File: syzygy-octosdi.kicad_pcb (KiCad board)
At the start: 4 copper layers, 100 x 50 mm, 211 parts, among them CN1 QTH-020-01-F-D-DP-A, J1 Conn_Coaxial, J2 Conn_Coaxial, J3 Conn_Coaxial, J4 Conn_Coaxial, J5 Conn_Coaxial, J6 Conn_Coaxial, J7 Conn_Coaxial, J8 Conn_Coaxial, J9 Conn_02x03_Odd_Even, U1 LMH0344SQE_NOPB, U10 GS2988-INE3, U11 STM32G031G8Ux, U2 LMH0344SQE_NOPB, U3 LMH0344SQE_NOPB, U4 LMH0344SQE_NOPB, U5 PCAL6416AHF, U6 PCAL6416AHF, U7 GS2988-INE3, U8 GS2988-INE3, U9 GS2988-INE3, X1 SX7DF148_500B20F30DNN

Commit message: finish routing
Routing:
- net +3V3: track 577.3 -> 703.0 mm, vias 48 -> 46
- net GND: track 137.2 -> 142.4 mm
- net /Outputs/SDI Out 3/SD/~{HD}: track 13.0 -> 14.6 mm

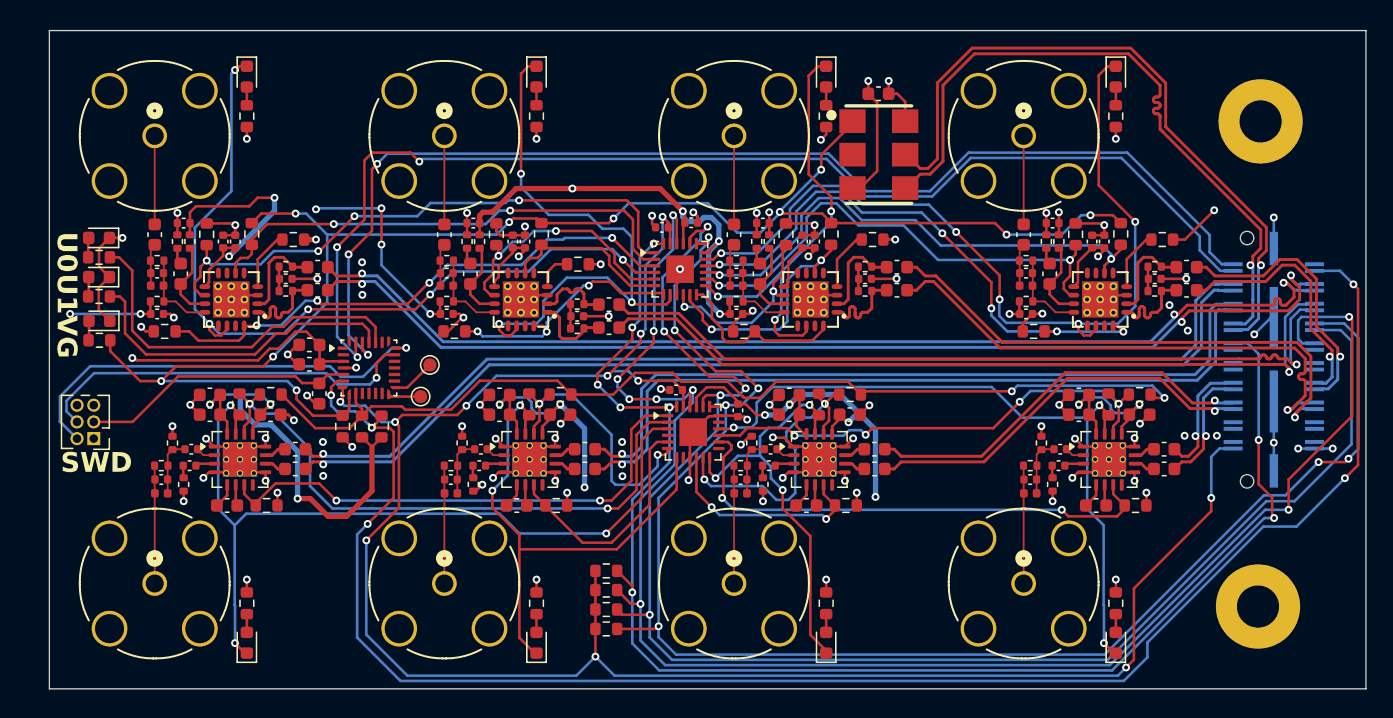
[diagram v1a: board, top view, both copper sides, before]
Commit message: fixes following review and more mounting holes
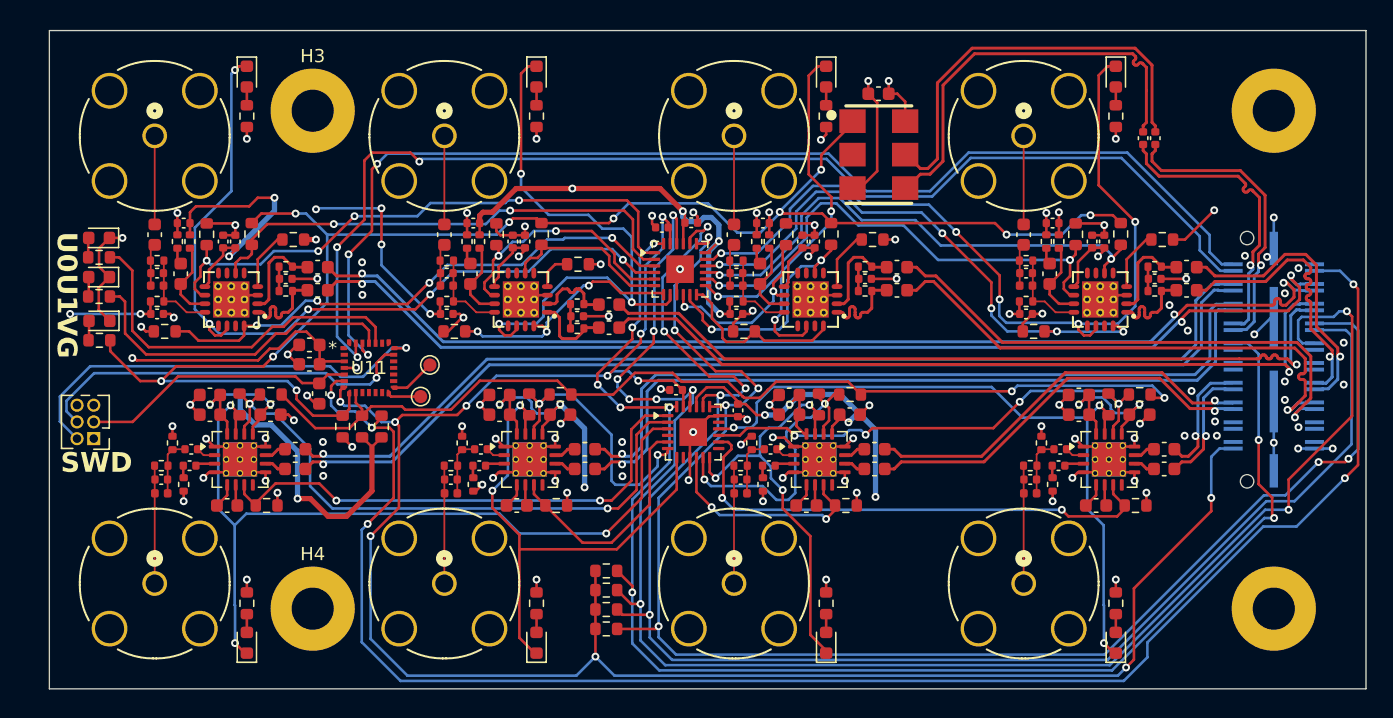
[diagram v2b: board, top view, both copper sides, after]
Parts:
- added C85: 10n, Capacitor_SMD:C_0402_1005Metric, F.Cu at (134.0, 58.2)
- added C86: 10n, Capacitor_SMD:C_0402_1005Metric, F.Cu at (133.1, 58.2)
- added H3: MountingHole_Pad, MountingHole:MountingHole_3.2mm_M3_Pad, F.Cu at (70.0, 56.1)
- added H4: MountingHole_Pad, MountingHole:MountingHole_3.2mm_M3_Pad, F.Cu at (70.0, 93.9)
- R36, R47, R58, R69: value 750 -> 750 1%
- U11: footprint Package_DFN_QFN:QFN-28_4x4mm_P0.5mm -> JLCImport:UFQFPN-28_STM
- moved H2 1.29 mm to (143.0, 56.1)
- moved H1 1.21 mm to (143.0, 93.9)
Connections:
- X1 pad 4: /REFCLK.P -> /REF+
- X1 pad 5: /REFCLK.N -> /REF-
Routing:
- net /REF-: track 0.00 -> 32.1 mm
- net /REF+: track 0.00 -> 32.0 mm
- net /REFCLK.N: track 52.3 -> 22.7 mm
- net /REFCLK.P: track 52.2 -> 22.7 mm
- net +3V3: track 703.0 -> 698.9 mm
- net /TX3.P: track 19.6 -> 21.9 mm
- net /TX3.N: track 21.0 -> 22.0 mm
- net GND: vias 78 -> 90

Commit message: add power led and test points
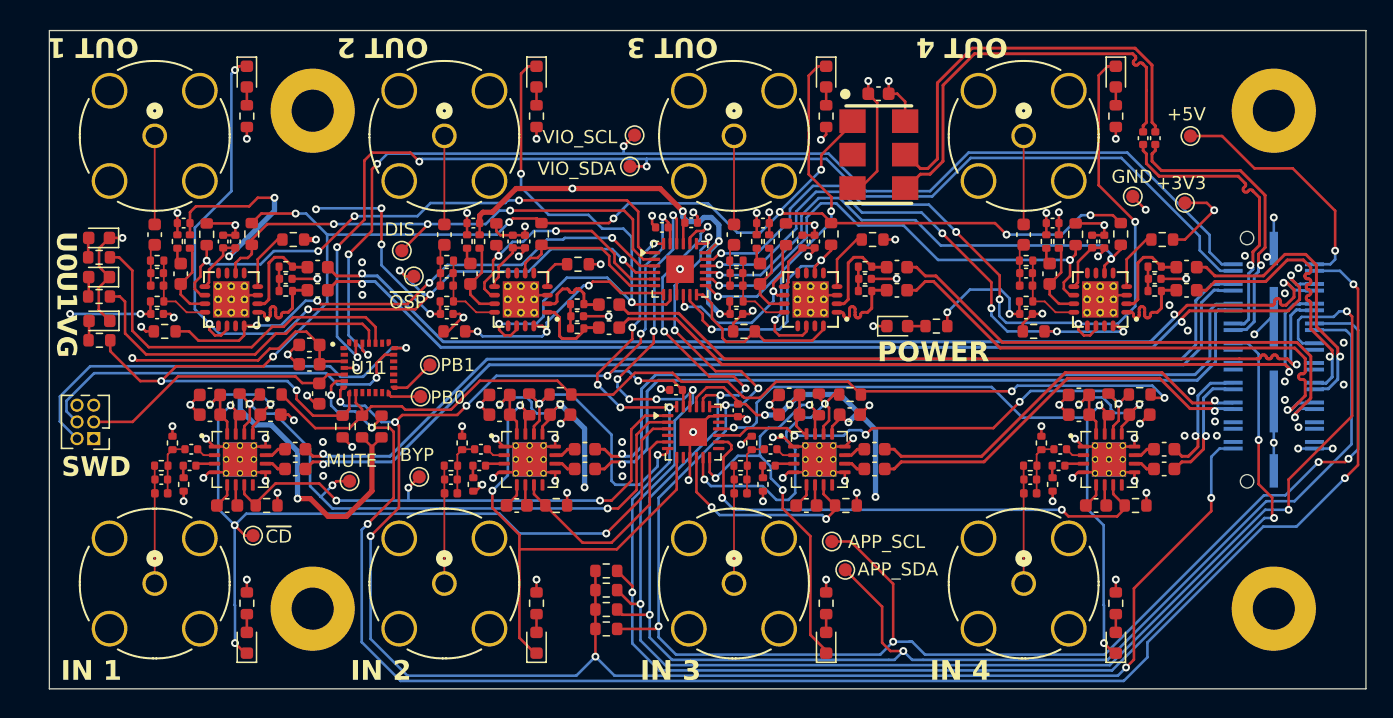
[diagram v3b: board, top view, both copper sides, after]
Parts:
- added D1: LED, LED_SMD:LED_0603_1608Metric, F.Cu at (114.4, 72.5)
- added R1: 1k, Resistor_SMD:R_0603_1608Metric, F.Cu at (117.4, 72.5)
- added TP1: TestPoint, TestPoint:TestPoint_Pad_D1.0mm, F.Cu at (109.4, 88.8)
- added TP10: TestPoint, TestPoint:TestPoint_Pad_D1.0mm, F.Cu at (65.5, 88.4)
- added TP11: TestPoint, TestPoint:TestPoint_Pad_D1.0mm, F.Cu at (76.8, 66.7)
- added TP12: TestPoint, TestPoint:TestPoint_Pad_D1.0mm, F.Cu at (77.7, 68.7)
- added TP2: TestPoint, TestPoint:TestPoint_Pad_D1.0mm, F.Cu at (94.5, 58.0)
- added TP3: TestPoint, TestPoint:TestPoint_Pad_D1.0mm, F.Cu at (94.1, 60.3)
- added TP4: TestPoint, TestPoint:TestPoint_Pad_D1.0mm, F.Cu at (136.7, 58.0)
- added TP5: TestPoint, TestPoint:TestPoint_Pad_D1.0mm, F.Cu at (136.2, 63.1)
- added TP6: TestPoint, TestPoint:TestPoint_Pad_D1.0mm, F.Cu at (132.3, 62.6)
- added TP7: TestPoint, TestPoint:TestPoint_Pad_D1.0mm, F.Cu at (110.5, 91.0)
- added TP8: TestPoint, TestPoint:TestPoint_Pad_D1.0mm, F.Cu at (78.1, 83.9)
- added TP9: TestPoint, TestPoint:TestPoint_Pad_D1.0mm, F.Cu at (72.8, 84.2)
- renumbered C85 to C1, C8 to C10, C9 to C11, C10 to C12, C11 to C13, C12 to C14, C13 to C15, C14 to C16, C15 to C17, C16 to C18, C17 to C19, C86 to C2, C18 to C20, C19 to C21, C20 to C22, C21 to C23, C22 to C24, C23 to C25, C24 to C26, C25 to C27, C26 to C28, C27 to C29, C1 to C3, C28 to C30, C29 to C31, C30 to C32, C31 to C33, C32 to C34, C33 to C35, C34 to C36, C35 to C37, C36 to C38, C37 to C39, C2 to C4, C38 to C40, C39 to C41, C40 to C42, C41 to C43, C42 to C44, C43 to C45, C44 to C46, C45 to C47, C46 to C48, C47 to C49, C3 to C5, C48 to C50, C49 to C51, C50 to C52, C51 to C53, C52 to C54, C53 to C55, C54 to C56, C55 to C57, C56 to C58, C57 to C59, C4 to C6, C58 to C60, C59 to C61, C60 to C62, C61 to C63, C62 to C64, C63 to C65, C64 to C66, C65 to C67, C66 to C68, C67 to C69, C5 to C7, C68 to C70, C69 to C71, C70 to C72, C71 to C73, C72 to C74, C73 to C75, C74 to C76, C75 to C77, C76 to C78, C77 to C79, C6 to C8, C78 to C80, C79 to C81, C80 to C82, C81 to C83, C82 to C84, C83 to C85, C84 to C86, C7 to C9, D9 to D10, D10 to D11, D11 to D12, D1 to D2, D2 to D3, D3 to D4, D4 to D5, D5 to D6, D6 to D7, D7 to D8, D8 to D9, H3 to H2, H2 to H3, R9 to R10, R10 to R11, R11 to R12, R12 to R13, R13 to R14, R14 to R15, R15 to R16, R16 to R17, R17 to R18, R18 to R19, R1 to R2, R19 to R20, R20 to R21, R21 to R22, R22 to R23, R23 to R24, R24 to R25, R25 to R26, R26 to R27, R27 to R28, R28 to R29, R2 to R3, R29 to R30, R30 to R31, R31 to R32, R32 to R33, R33 to R34, R34 to R35, R35 to R36, R36 to R37, R37 to R38, R38 to R39, R3 to R4, R39 to R40, R40 to R41, R41 to R42, R42 to R43, R43 to R44, R44 to R45, R45 to R46, R46 to R47, R47 to R48, R48 to R49, R4 to R5, R49 to R50, R50 to R51, R51 to R52, R52 to R53, R53 to R54, R54 to R55, R55 to R56, R56 to R57, R57 to R58, R58 to R59, R5 to R6, R59 to R60, R60 to R61, R61 to R62, R62 to R63, R63 to R64, R64 to R65, R65 to R66, R66 to R67, R67 to R68, R68 to R69, R6 to R7, R69 to R70, R70 to R71, R71 to R72, R72 to R73, R73 to R74, R74 to R75, R75 to R76, R76 to R77, R77 to R78, R78 to R79, R7 to R8, R79 to R80, R80 to R81, R81 to R82, R82 to R83, R8 to R9, TP1 to TP13, TP2 to TP14
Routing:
- net +5V: track 0.00 -> 18.8 mm, vias 0 -> 1
- net /I2C.SCL: track 117.6 -> 128.9 mm, vias 7 -> 8
- net +3V3: track 698.9 -> 709.3 mm, vias 46 -> 47
- net /I2C.SDA: track 119.1 -> 128.2 mm, vias 5 -> 6
- net /Outputs/SDI Out 1/~{OSP}: track 61.9 -> 66.3 mm, vias 5 -> 6
- net /Outputs/SDI Out 1/~{DISABLE}: track 37.9 -> 40.8 mm, vias 2 -> 3
- net /Inputs/SDI In 1/MUTE: track 46.5 -> 49.2 mm, vias 2 -> 3
- net GND: track 142.4 -> 144.8 mm, vias 90 -> 92
- net /Inputs/SDI In 1/BYPASS: track 39.5 -> 41.6 mm, vias 2 -> 3
- net /VIO_I2C.SDA: track 90.8 -> 92.6 mm, vias 3 -> 4
- net /VIO_I2C.SCL: track 89.2 -> 90.9 mm, vias 3 -> 4
- net /Inputs/SDI In 1/~{CD}: track 62.5 -> 64.2 mm, vias 3 -> 4
- net Net-(D1-A): track 0.00 -> 1.36 mm
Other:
- board text added: "+3V3"
- board text added: "+5V"
- board text added: "APP_SCL"
- board text added: "APP_SDA"
- board text added: "BYP"
- board text added: "DIS"
- board text added: "GND"
- board text added: "IN 1"
- board text added: "IN 2"
- board text added: "IN 3"
- board text added: "IN 4"
- board text added: "MUTE"
- board text added: "OUT 1"
- board text added: "OUT 2"
- board text added: "OUT 3"
- board text added: "OUT 4"
- board text added: "PB0"
- board text added: "PB1"
- board text added: "POWER"
- board text added: "VIO_SCL"
- board text added: "VIO_SDA"
- board text added: "~{CD}"
- board text added: "~{OSP}"

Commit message: add labels and syzygy info
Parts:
- added G***: LOGO, Syzygy:SYZYGY_Logo, F.Cu at (142.4, 68.6)
- added REF**: SYZYGY_STD_Logo, Syzygy:SYZYGY_TXR4_Logo, F.Cu at (141.2, 82.2)
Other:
- board text added: "POD-OCTOSDI v1"

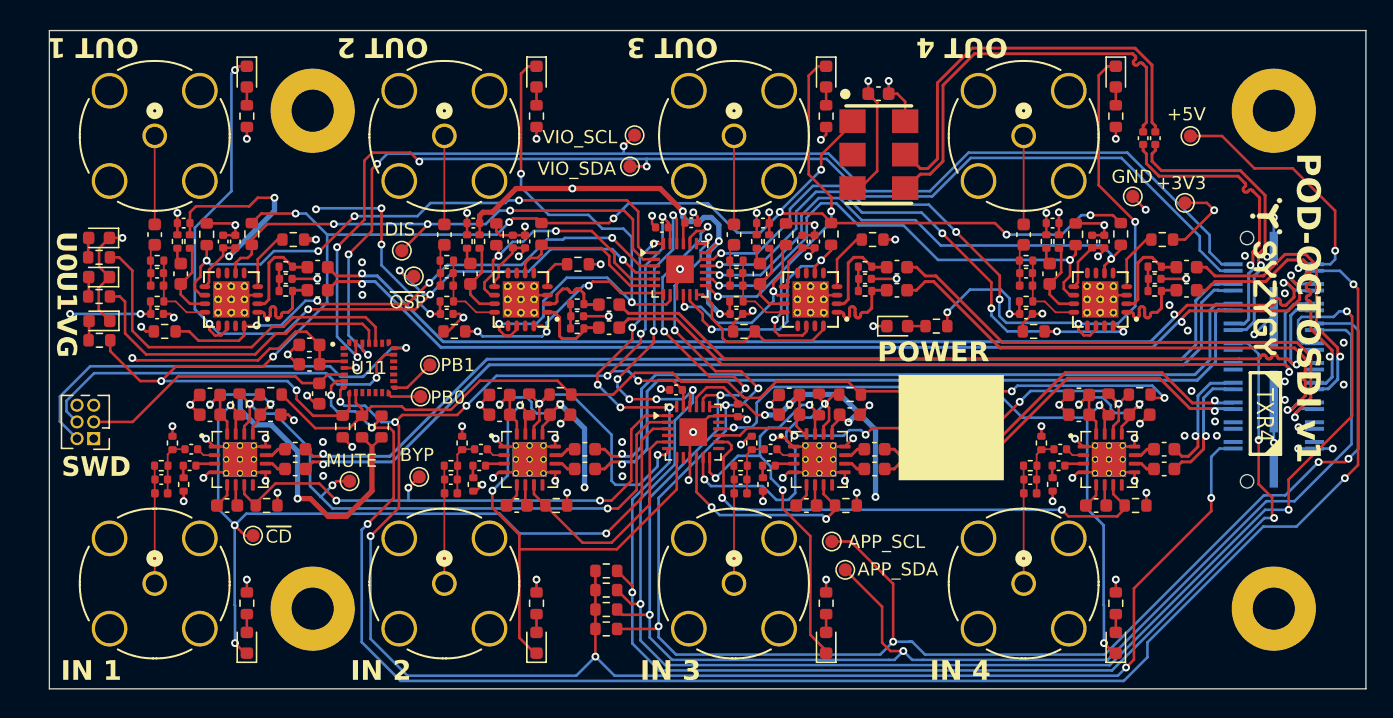
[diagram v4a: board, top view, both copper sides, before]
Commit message: check against jlcpcb capabilities
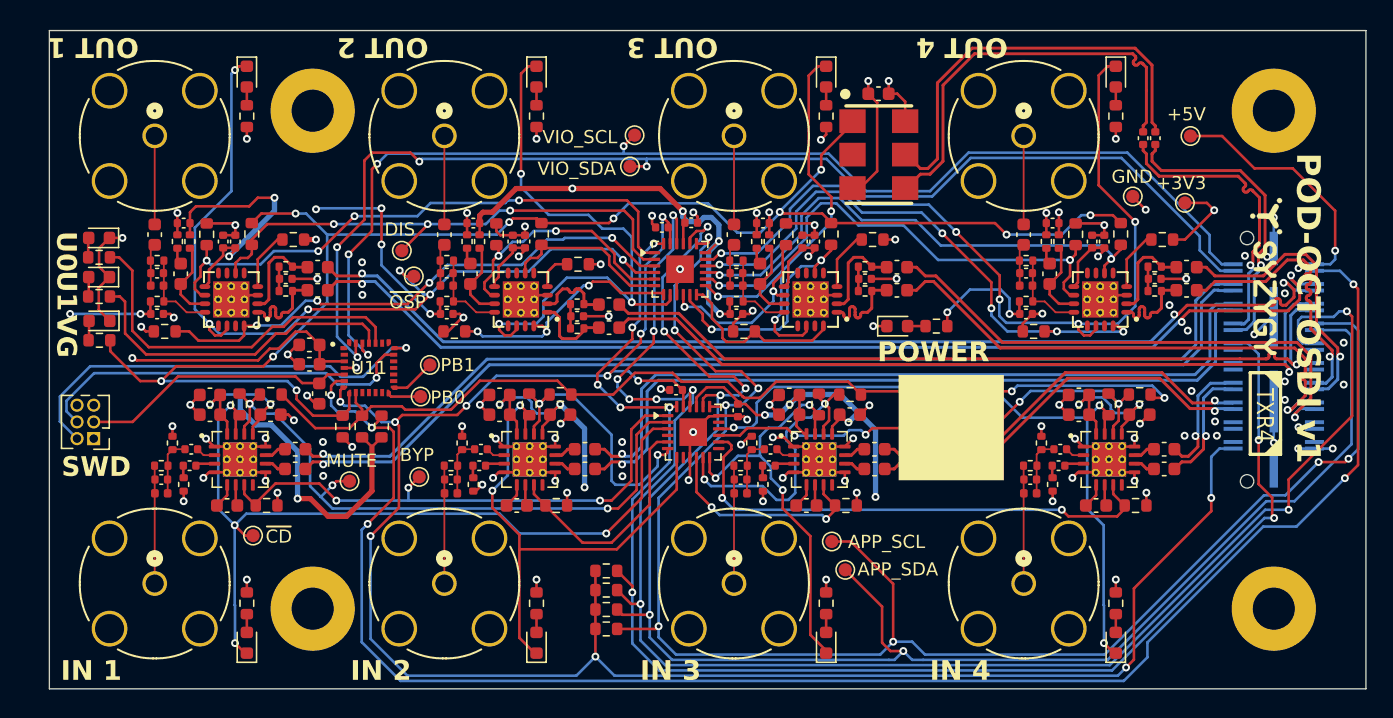
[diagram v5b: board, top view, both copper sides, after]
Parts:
- J1, J2, J3, J4, J5, J6, J7, J8: value Conn_Coaxial -> Conn_BNC
